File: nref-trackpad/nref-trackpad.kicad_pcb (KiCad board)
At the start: 2 copper layers, 90.5 x 15 mm, 11 parts, among them J1 Conn_01x06_Female, J2 Conn_01x06_Female, SW1 SW_Push, SW2 SW_Push, SW3 SW_Push, U1 PCAL6416AHF

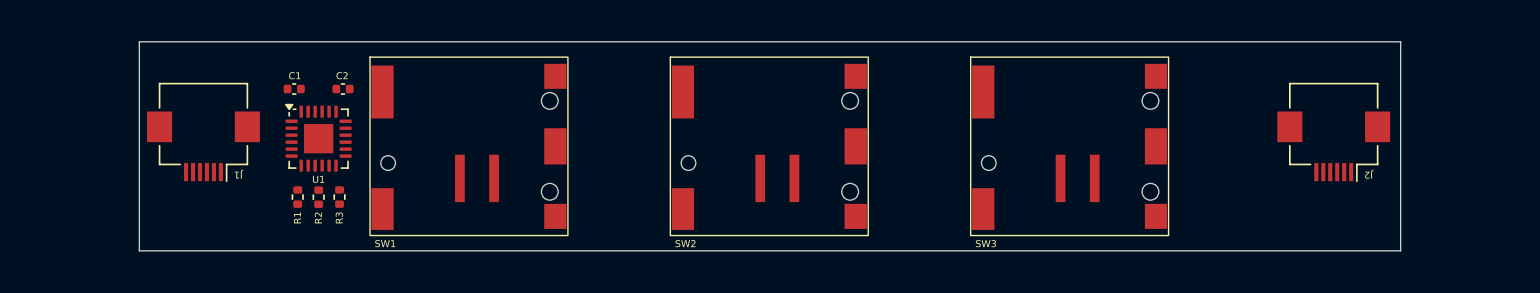
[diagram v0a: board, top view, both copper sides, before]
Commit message: trackpad: add first button board design d-1
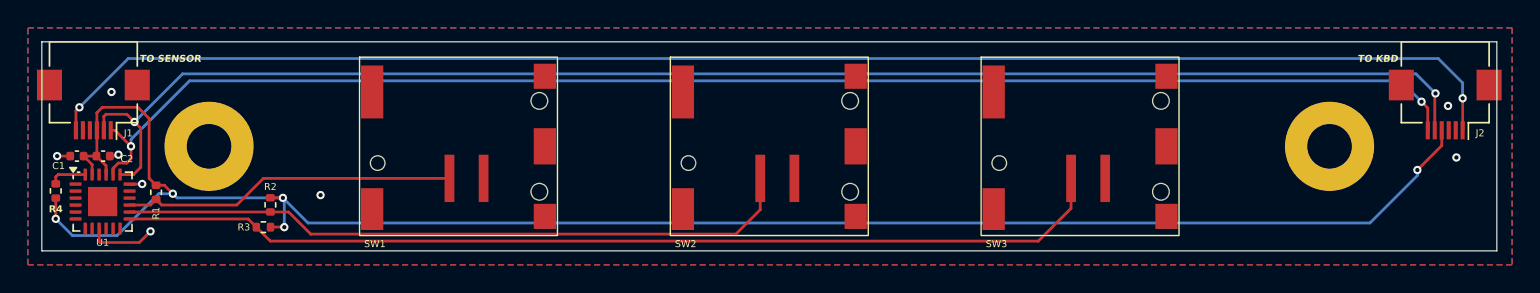
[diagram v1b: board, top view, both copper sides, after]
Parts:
- added H1: MountingHole_Pad, MountingHole:MountingHole_3.2mm_M3_Pad, F.Cu at (102.5, 81.5)
- added H2: MountingHole_Pad, MountingHole:MountingHole_3.2mm_M3_Pad, F.Cu at (182.9, 81.5)
- added R4: 4.7k, Resistor_SMD:R_0402_1005Metric, F.Cu at (91.5, 84.7)
- moved C2 17.9 mm to (94.9, 82.2), turned to 0 degrees
- moved C1 16.3 mm to (93.0, 82.2), turned to 180 degrees
- moved U1 16.1 mm to (94.9, 85.5)
- moved R1 10.2 mm to (98.7, 84.8)
- moved J2 8.54 mm to (191.2, 78.5)
- moved J1 8.45 mm to (94.2, 78.5)
- moved R3 5.87 mm to (106.4, 87.3), turned to 180 degrees
- moved R2 3.51 mm to (106.9, 85.7)
- moved SW1 0.75 mm to (120.4, 81.5)
- moved SW3 0.75 mm to (165.0, 81.5)
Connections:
- R1 pad 2: Net-(U1-P0_0) -> Net-(U1-P1_5)
- R2 pad 2: Net-(U1-P0_1) -> Net-(U1-P1_4)
- R3 pad 2: Net-(U1-P0_2) -> Net-(U1-P1_3)
- SW1 pad 1: Net-(U1-P0_0) -> Net-(U1-P1_5)
- SW2 pad 1: Net-(U1-P0_1) -> Net-(U1-P1_4)
- SW3 pad 1: Net-(U1-P0_2) -> Net-(U1-P1_3)
- U1 pad 1: Net-(U1-P0_0) -> unconnected-(U1-P0_0-Pad1)
- U1 pad 13: unconnected-(U1-P1_3-Pad13) -> Net-(U1-P1_3)
- U1 pad 14: unconnected-(U1-P1_4-Pad14) -> Net-(U1-P1_4)
- U1 pad 15: unconnected-(U1-P1_5-Pad15) -> Net-(U1-P1_5)
- U1 pad 18: unconnected-(U1-ADDR-Pad18) -> GND
- U1 pad 2: Net-(U1-P0_1) -> unconnected-(U1-P0_1-Pad2)
- U1 pad 24: unconnected-(U1-~{RESET}-Pad24) -> Net-(U1-~{RESET})
- U1 pad 3: Net-(U1-P0_2) -> unconnected-(U1-P0_2-Pad3)
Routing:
- net +3V3: track 0.00 -> 129.2 mm, vias 0 -> 5
- net SCL: track 0.00 -> 106.7 mm, vias 0 -> 2
- net RDY: track 0.00 -> 106.6 mm, vias 0 -> 2
- net SDA: track 0.00 -> 102.5 mm, vias 0 -> 2
- net Net-(U1-P1_3): track 0.00 -> 71.3 mm
- net Net-(U1-P1_4): track 0.00 -> 48.9 mm
- net Net-(U1-P1_5): track 0.00 -> 24.1 mm
- net GND: track 0.00 -> 7.47 mm, vias 0 -> 8
- net Net-(U1-~{RESET}): track 0.00 -> 2.67 mm
- added copper zone on B.Cu, net GND
- added copper zone on F.Cu, net GND
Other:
- board size 90.5 x 15 mm -> 104.4 x 15 mm
- board text added: "TO KBD"
- board text added: "TO SENSOR"

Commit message: trackpad buttons: move left and right button further out
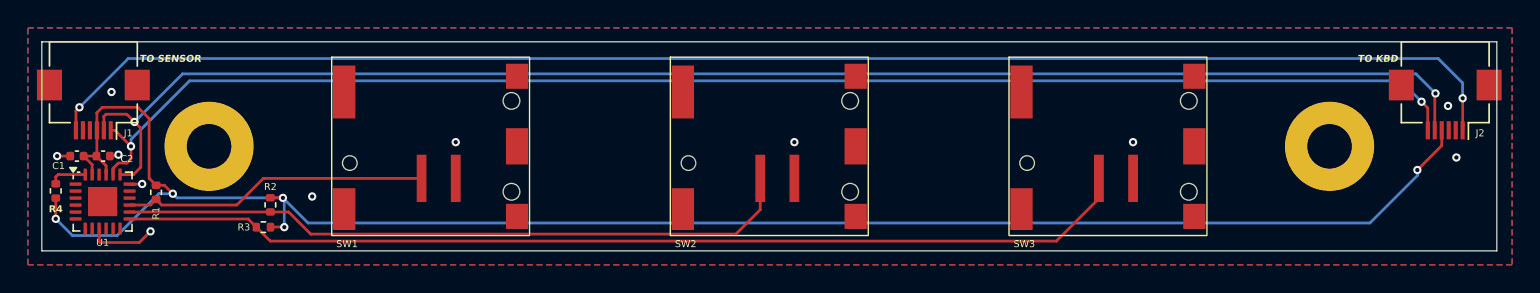
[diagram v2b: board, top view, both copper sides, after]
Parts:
- moved SW1 2.00 mm to (118.4, 81.5)
- moved SW3 2.00 mm to (167.0, 81.5)
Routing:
- net Net-(U1-P1_5): track 24.1 -> 22.1 mm
- net Net-(U1-P1_3): track 71.3 -> 72.9 mm
- net GND: vias 8 -> 11
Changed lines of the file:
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@@
 			(drillshape 0)
 			(scaleselection 1)
-			(outputdirectory "nref-trackpad-d1")
+			(outputdirectory "nref-trackpad-d2")
 		)
 	)
@@
 		)
 		(property "Value" "4.7k"
-			(at 0 1.17 360)
+			(at 0 1.17 0)
 			(layer "F.Fab")
 			(effects
@@
 		)
 		(fp_text user "${REFERENCE}"
-			(at 0 0 360)
+			(at 0 0 0)
 			(layer "F.Fab")
 			(effects
@@
 	(footprint "Cherry_ULP:Cherry_ULP_SMD"
 		(layer "F.Cu")
-		(at 165 81.5)
+		(at 167 81.5)
 		(property "Reference" "SW3"
 			(at -6 7 0)
@@
 			(polygon
 				(pts
-					(xy 163.8 85.7) (xy 160 85.7) (xy 160 83.7) (xy 163.8 83.7)
+					(xy 165.8 85.7) (xy 162 85.7) (xy 162 83.7) (xy 165.8 83.7)
 				)
 			)
@@
 		)
 		(property "Value" "0.1uF"
-			(at 0 1.16 360)
+			(at 0 1.16 0)
 			(layer "F.Fab")
 			(effects
@@
 		)
 		(fp_text user "${REFERENCE}"
-			(at 0 0 360)
+			(at 0 0 0)
 			(layer "F.Fab")
 			(effects
@@
 	(footprint "Cherry_ULP:Cherry_ULP_SMD"
 		(layer "F.Cu")
-		(at 120.4 81.5)
+		(at 118.4 81.5)
 		(property "Reference" "SW1"
 			(at -6 7 0)
@@
 			(polygon
 				(pts
-					(xy 119.2 85.7) (xy 115.4 85.7) (xy 115.4 83.7) (xy 119.2 83.7)
+					(xy 117.2 85.7) (xy 113.4 85.7) (xy 113.4 83.7) (xy 117.2 83.7)
 				)
 			)
@@
 		)
 		(property "Value" "0.1uF"
-			(at 0 1.16 360)
+			(at 0 1.16 0)
 			(layer "F.Fab")
 			(effects
@@
 		)
 		(fp_text user "${REFERENCE}"
-			(at 0 0 360)
+			(at 0 0 0)
 			(layer "F.Fab")
 			(effects
@@
 	)
 	(via
-		(at 110.5 85)
+		(at 120.2 81.2)
+		(size 0.6)
+		(drill 0.3)
+		(layers "F.Cu" "B.Cu")
+		(net 1)
+	)
+	(via
+		(at 109.9 85.1)
 		(size 0.6)
 		(drill 0.3)
@@
 	)
 	(via
+		(at 144.5 81.2)
+		(size 0.6)
+		(drill 0.3)
+		(layers "F.Cu" "B.Cu")
+		(net 1)
+	)
+	(via
 		(at 96 82.1)
 		(size 0.6)
@@
 	)
 	(via
+		(at 168.8 81.2)
+		(size 0.6)
+		(drill 0.3)
+		(layers "F.Cu" "B.Cu")
+		(net 1)
+	)
+	(via
 		(at 95.5 77.6)
 		(size 0.6)
@@
 	)
 	(segment
-		(start 99.1025 85.7125)
-		(end 104.4875 85.7125)
+		(start 96.8 85.7125)
+		(end 98.2975 85.7125)
 		(width 0.2)
 		(layer "F.Cu")
@@
 	)
 	(segment
-		(start 106.4 83.8)
-		(end 119.75 83.8)
+		(start 104.4875 85.7125)
+		(end 106.4 83.8)
 		(width 0.2)
 		(layer "F.Cu")
@@
 	)
 	(segment
-		(start 104.4875 85.7125)
-		(end 106.4 83.8)
+		(start 98.7 85.31)
+		(end 99.1025 85.7125)
 		(width 0.2)
 		(layer "F.Cu")
@@
 	)
 	(segment
-		(start 96.8 85.7125)
-		(end 98.2975 85.7125)
+		(start 98.2975 85.7125)
+		(end 98.7 85.31)
 		(width 0.2)
 		(layer "F.Cu")
@@
 	)
 	(segment
-		(start 98.7 85.31)
-		(end 99.1025 85.7125)
+		(start 106.4 83.8)
+		(end 117.75 83.8)
 		(width 0.2)
 		(layer "F.Cu")
@@
 	)
 	(segment
-		(start 98.2975 85.7125)
-		(end 98.7 85.31)
+		(start 99.1025 85.7125)
+		(end 104.4875 85.7125)
 		(width 0.2)
 		(layer "F.Cu")
@@
 	)
 	(segment
-		(start 106.9 88.3)
-		(end 162 88.3)
+		(start 163.3 88.3)
+		(end 166.35 85.25)
 		(width 0.2)
 		(layer "F.Cu")
@@
 	)
 	(segment
-		(start 162 88.3)
-		(end 164.35 85.95)
+		(start 96.8 86.7125)
+		(end 105.3125 86.7125)
 		(width 0.2)
 		(layer "F.Cu")
@@
 	)
 	(segment
-		(start 164.35 85.95)
-		(end 164.35 83.8)
+		(start 106.9 88.3)
+		(end 163.3 88.3)
 		(width 0.2)
 		(layer "F.Cu")
@@
 	)
 	(segment
-		(start 96.8 86.7125)
-		(end 105.3125 86.7125)
+		(start 166.35 85.25)
+		(end 166.35 83.8)
 		(width 0.2)
 		(layer "F.Cu")
